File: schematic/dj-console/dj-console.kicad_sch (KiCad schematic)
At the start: 0 parts

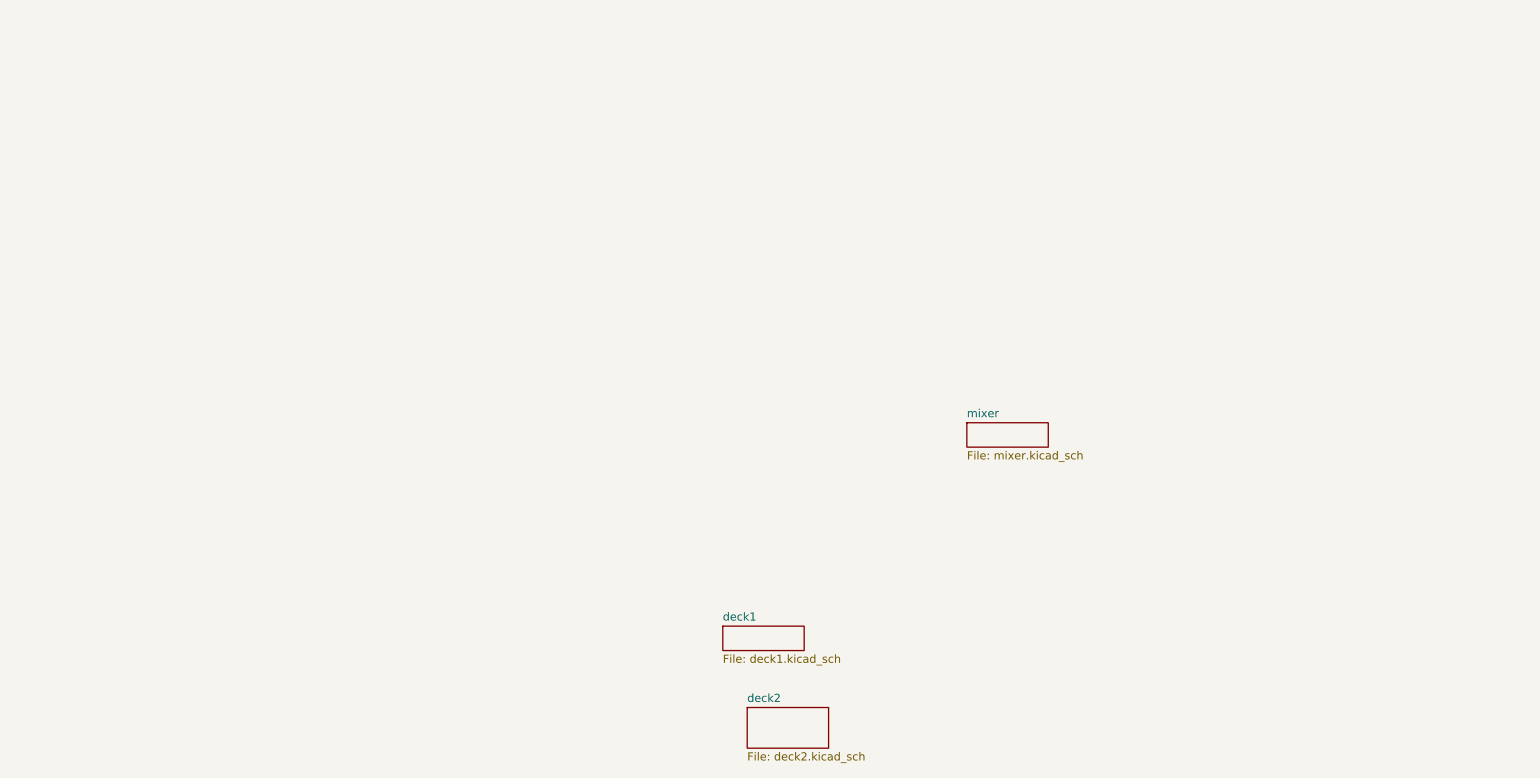
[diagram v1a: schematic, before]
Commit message: Finished DECK circuitry -> to be reviewed; Created hierarchical sheets to avoid redundancy
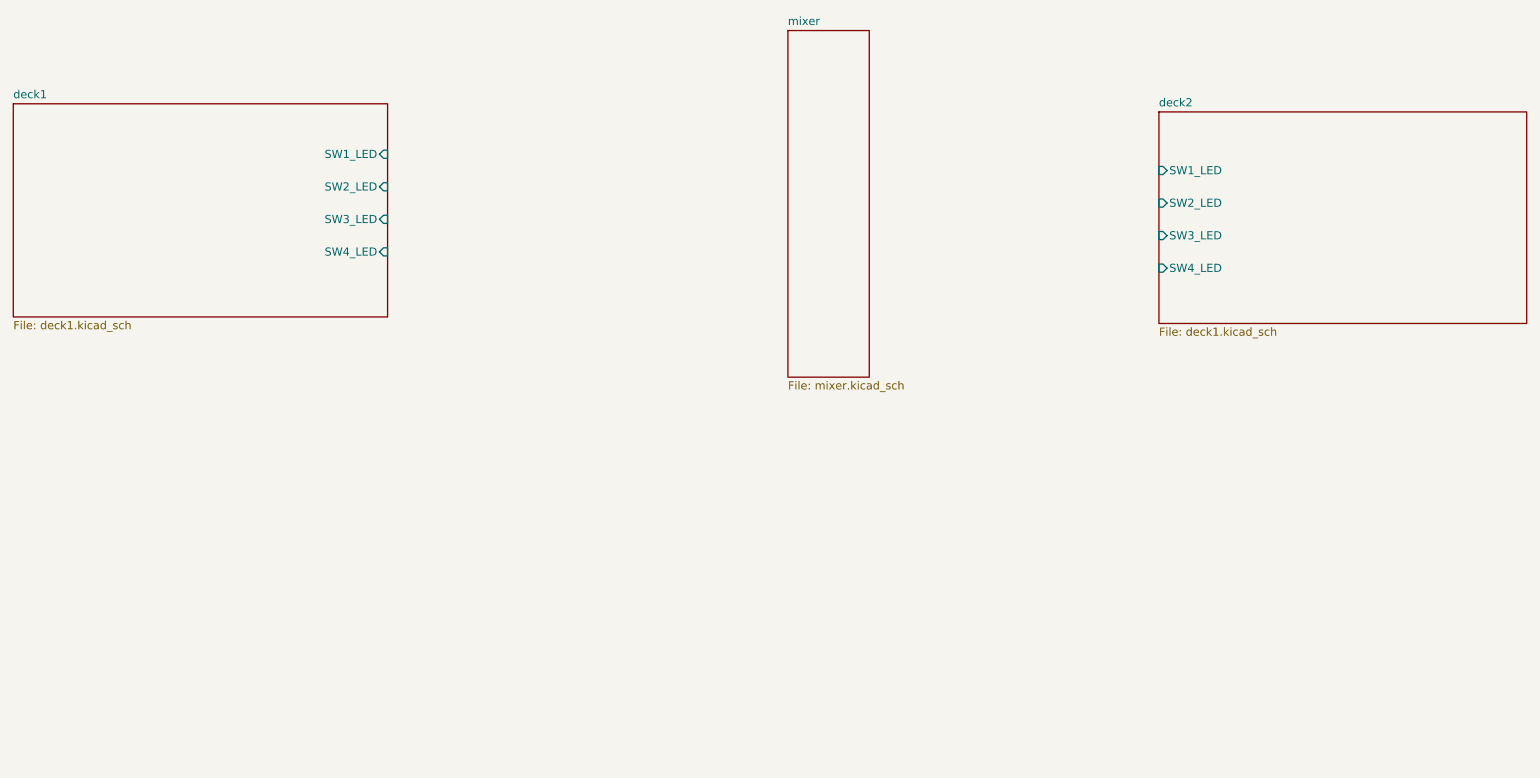
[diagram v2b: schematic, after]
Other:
- sheet deck1 ports: added SW1_LED, SW2_LED, SW3_LED, SW4_LED; removed none
- sheet deck2: file deck2.kicad_sch -> deck1.kicad_sch
- sheet deck2 ports: added SW1_LED, SW2_LED, SW3_LED, SW4_LED; removed none
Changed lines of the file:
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@@
 	)
 	(sheet
-		(at 173.99 135.89)
-		(size 12.7 3.81)
+		(at 203.962 87.376)
+		(size 57.404 33.02)
 		(exclude_from_sim no)
 		(in_bom yes)
@@
 			(color 0 0 0 0)
 		)
-		(property "Sheetname" "mixer"
-			(at 173.99 135.1784 0)
+		(property "Sheetname" "deck2"
+			(at 203.962 86.6644 0)
 			(show_name no)
 			(do_not_autoplace no)
@@
 			)
 		)
-		(property "Sheetfile" "mixer.kicad_sch"
-			(at 173.99 140.2846 0)
+		(property "Sheetfile" "deck1.kicad_sch"
+			(at 203.962 120.9806 0)
 			(show_name no)
 			(do_not_autoplace no)
@@
 				)
 				(justify left top)
+			)
+		)
+		(pin "SW1_LED" input
+			(at 203.962 96.52 180)
+			(effects
+				(font
+					(size 1.27 1.27)
+				)
+				(justify left)
+			)
+		)
+		(pin "SW2_LED" input
+			(at 203.962 101.6 180)
+			(effects
+				(font
+					(size 1.27 1.27)
+				)
+				(justify left)
+			)
+		)
+		(pin "SW3_LED" input
+			(at 203.962 106.68 180)
+			(effects
+				(font
+					(size 1.27 1.27)
+				)
+				(justify left)
+			)
+		)
+		(pin "SW4_LED" input
+			(at 203.962 111.76 180)
+			(effects
+				(font
+					(size 1.27 1.27)
+				)
+				(justify left)
 			)
 		)
@@
 			(project "dj-console"
 				(path "/cbea8acf-e301-41c4-99fc-3eb7e47427af"
-					(page "4")
+					(page "3")
 				)
 			)
@@
 	)
 	(sheet
-		(at 139.7 180.34)
-		(size 12.7 6.35)
+		(at 146.05 74.676)
+		(size 12.7 54.102)
 		(exclude_from_sim no)
 		(in_bom yes)
@@
 			(color 0 0 0 0)
 		)
-		(property "Sheetname" "deck2"
-			(at 139.7 179.6284 0)
+		(property "Sheetname" "mixer"
+			(at 146.05 73.9644 0)
 			(show_name no)
 			(do_not_autoplace no)
@@
 			)
 		)
-		(property "Sheetfile" "deck2.kicad_sch"
-			(at 139.7 187.2746 0)
+		(property "Sheetfile" "mixer.kicad_sch"
+			(at 146.05 129.3626 0)
 			(show_name no)
 			(do_not_autoplace no)
@@
 			(project "dj-console"
 				(path "/cbea8acf-e301-41c4-99fc-3eb7e47427af"
-					(page "3")
+					(page "4")
 				)
 			)
@@
 	)
 	(sheet
-		(at 135.89 167.64)
-		(size 12.7 3.81)
+		(at 25.146 86.106)
+		(size 58.42 33.274)
 		(exclude_from_sim no)
 		(in_bom yes)
@@
 		)
 		(property "Sheetname" "deck1"
-			(at 135.89 166.9284 0)
+			(at 25.146 85.3944 0)
 			(show_name no)
 			(do_not_autoplace no)
@@
 		)
 		(property "Sheetfile" "deck1.kicad_sch"
-			(at 135.89 172.0346 0)
+			(at 25.146 119.9646 0)
 			(show_name no)
 			(do_not_autoplace no)
@@
 			)
 		)
+		(pin "SW1_LED" input
+			(at 83.566 93.98 0)
+			(effects
+				(font
+					(size 1.27 1.27)
+				)
+				(justify right)
+			)
+		)
+		(pin "SW2_LED" input
+			(at 83.566 99.06 0)
+			(effects
+				(font
+					(size 1.27 1.27)
+				)
+				(justify right)
+			)
+		)
+		(pin "SW3_LED" input
+			(at 83.566 104.14 0)
+			(effects
+				(font
+					(size 1.27 1.27)
+				)
+				(justify right)
+			)
+		)
+		(pin "SW4_LED" input
+			(at 83.566 109.22 0)
+			(effects
+				(font
+					(size 1.27 1.27)
+				)
+				(justify right)
+			)
+		)

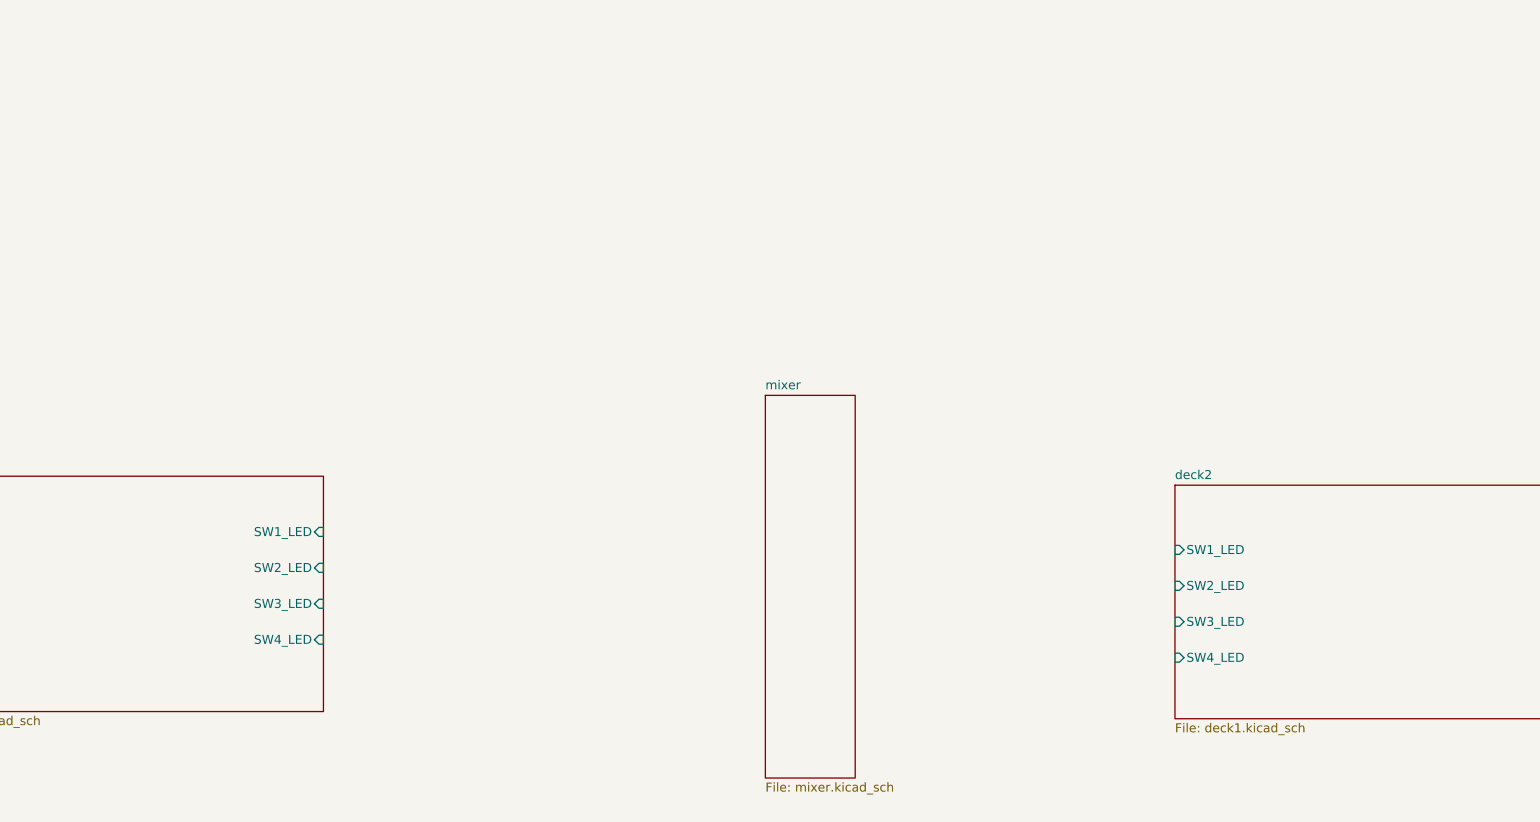
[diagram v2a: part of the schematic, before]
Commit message: Created first version of mixer circuit and added tempo sliders on decks
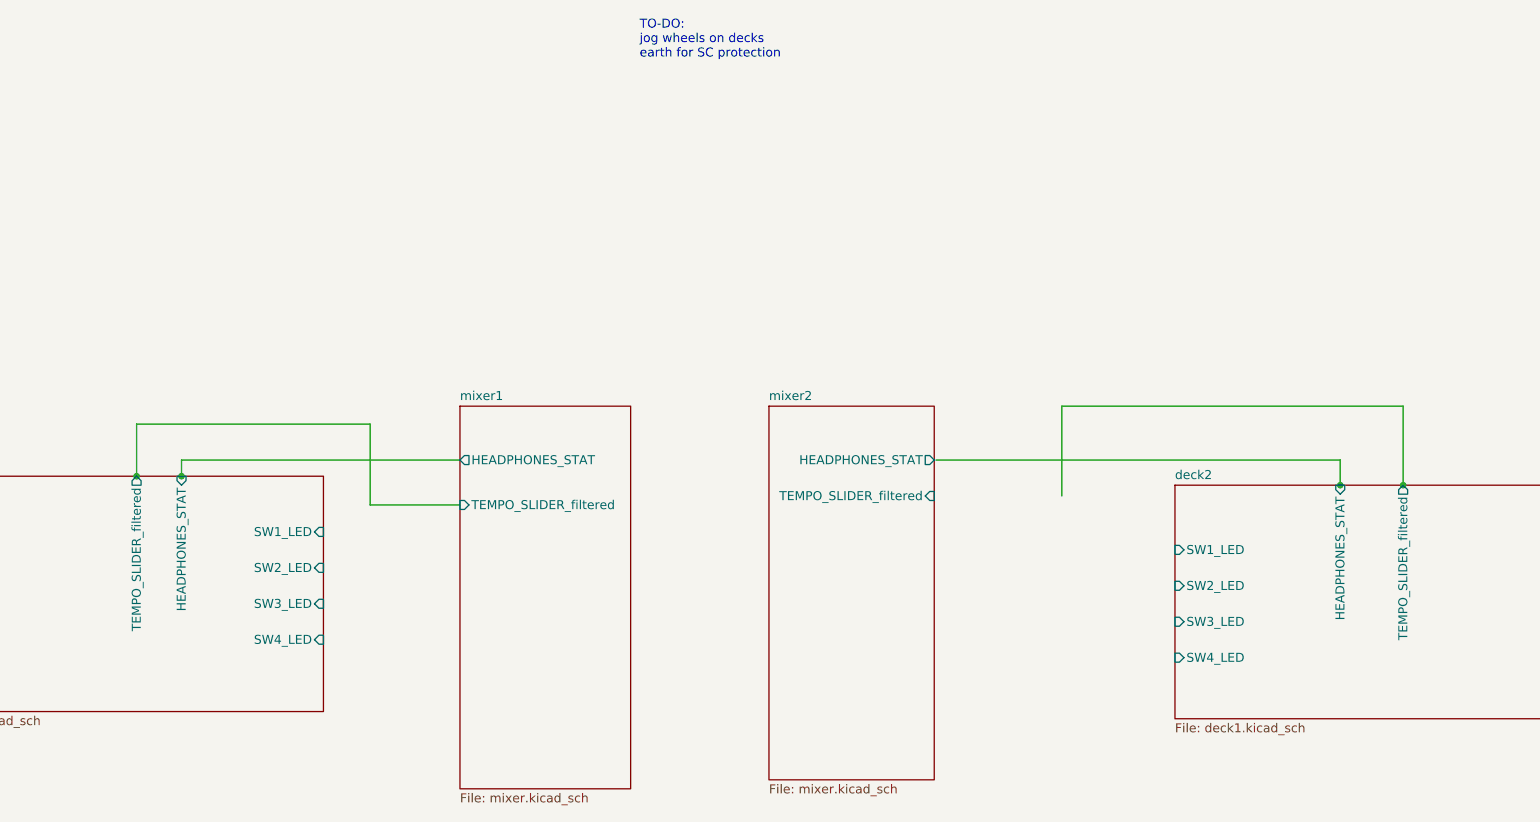
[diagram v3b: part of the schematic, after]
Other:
- sheet mixer renamed mixer1
- added sheet mixer2 (mixer.kicad_sch)
- sheet deck1 ports: added HEADPHONES_STAT, TEMPO_SLIDER_filtered; removed none
- sheet deck2 ports: added HEADPHONES_STAT, TEMPO_SLIDER_filtered; removed none
- sheet mixer1 ports: added HEADPHONES_STAT, TEMPO_SLIDER_filtered; removed none
- note added: "TO-DO: jog wheels on decks earth for SC protection"

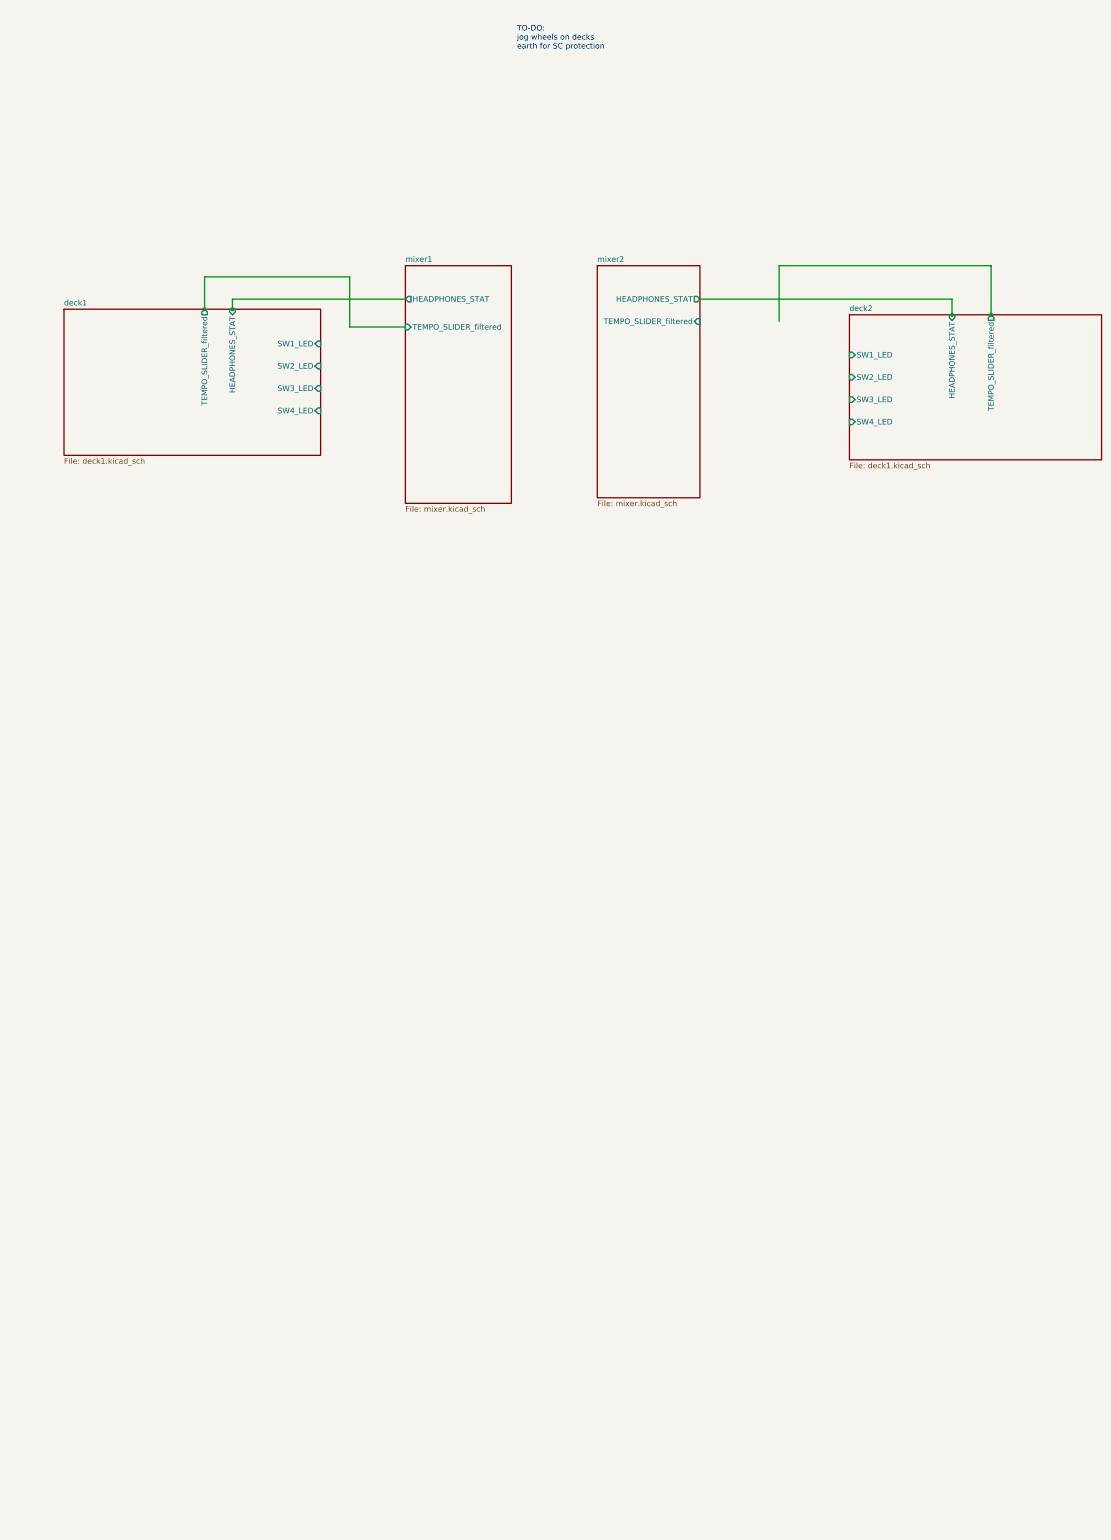
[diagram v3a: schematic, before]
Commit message: Added MASTER and HEADPHONES gain together with crossfader slider
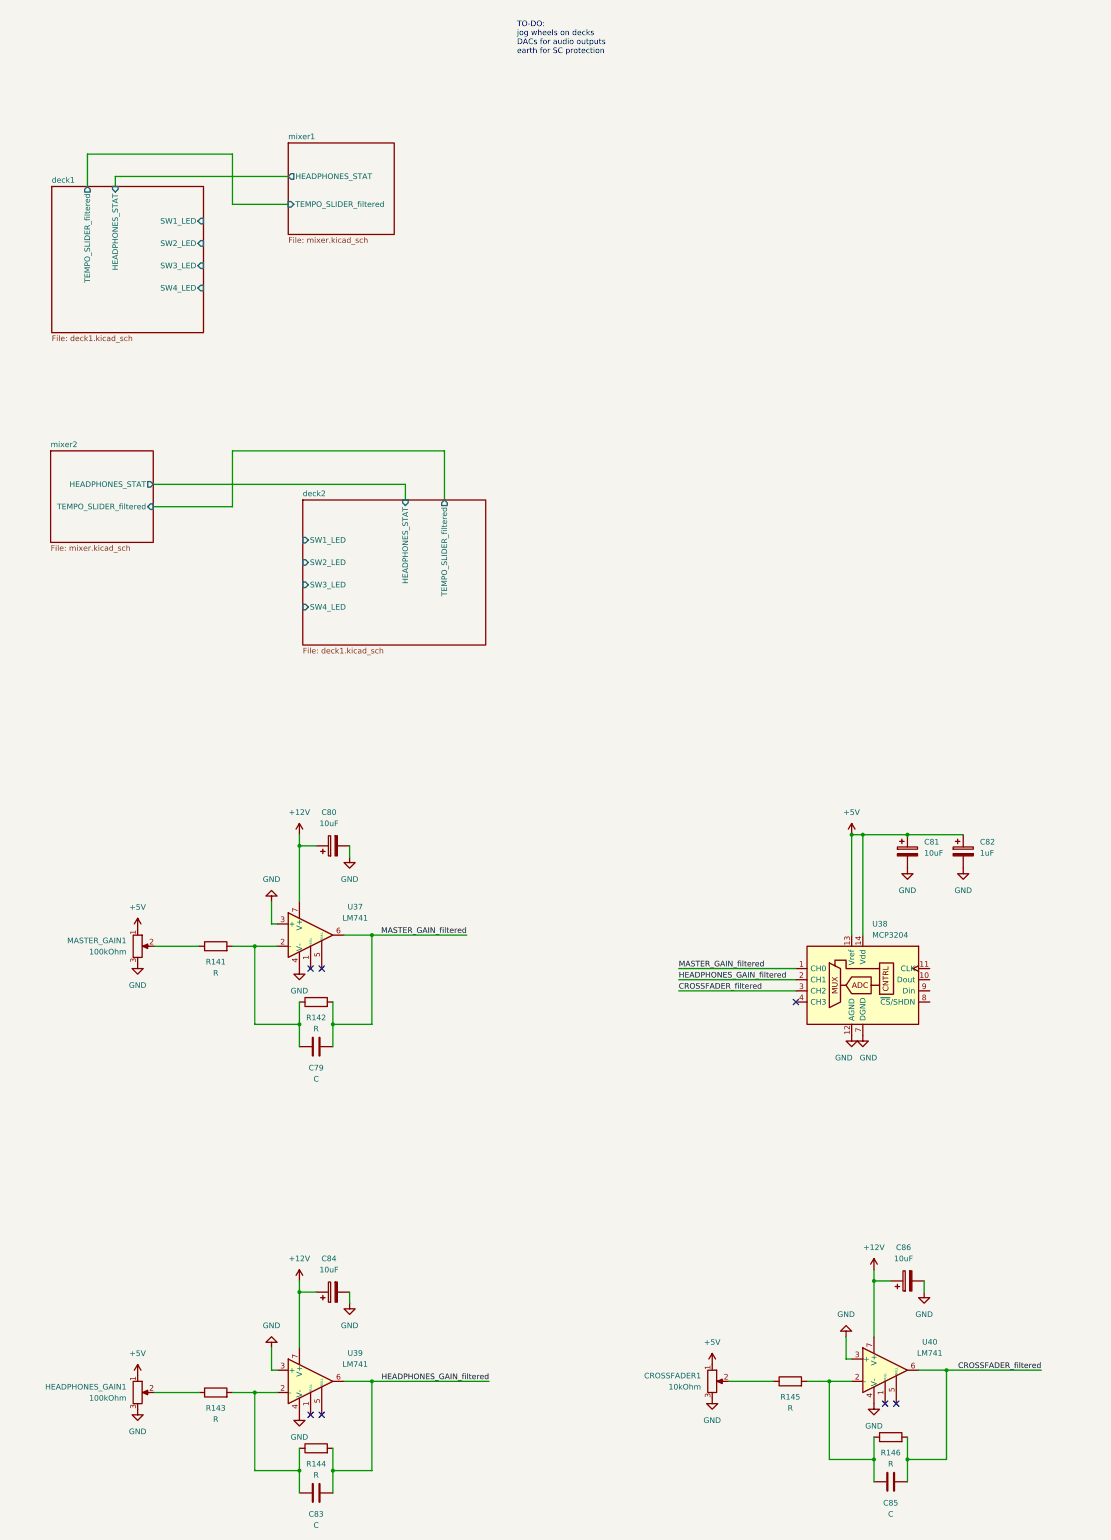
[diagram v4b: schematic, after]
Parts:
- added C79, C83, C85: C, symbol Device:C
- added C80, C81, C84, C86: 10uF, symbol Device:C_Polarized
- added C82: 1uF, symbol Device:C_Polarized
- added CROSSFADER1: 10kOhm, symbol Device:R_Potentiometer
- added HEADPHONES_GAIN1, MASTER_GAIN1: 100kOhm, symbol Device:R_Potentiometer
- added R141, R142, R143, R144, R145, R146: R, symbol Device:R
- added U37, U39, U40: LM741, symbol Amplifier_Operational:LM741
- added U38: MCP3204, symbol Analog_ADC:MCP3204
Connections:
- new net: C85.2, R145.2, R146.1, U40.2 (-)
- new net: HEADPHONES_GAIN1.2, R143.1
- new net: C83.2, R143.2, R144.1, U39.2 (-)
- new net: CROSSFADER1.2, R145.1
- new net: C79.2, R141.2, R142.1, U37.2 (-)
- new net: MASTER_GAIN1.2, R141.1
- new net +12V: C80.1, C84.1, C86.1, U37.7 (V+), U39.7 (V+), U40.7 (V+)
- new net +5V: C81.1, C82.1, CROSSFADER1.1, HEADPHONES_GAIN1.1, MASTER_GAIN1.1, U38.13 (Vref), U38.14 (Vdd)
- new net CROSSFADER_filtered: C85.1, R146.2, U38.3 (CH2), U40.6
- new net GND: C80.2, C81.2, C82.2, C84.2, C86.2, CROSSFADER1.3, HEADPHONES_GAIN1.3, MASTER_GAIN1.3, U37.3 (+), U37.4 (V-), U38.12 (AGND), U38.7 (DGND), U39.3 (+), U39.4 (V-), U40.3 (+), U40.4 (V-)
- new net HEADPHONES_GAIN_filtered: C83.1, R144.2, U38.2 (CH1), U39.6
- new net MASTER_GAIN_filtered: C79.1, R142.2, U37.6, U38.1 (CH0)
- no-connect marks 0 -> 7
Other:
- note added: "TO-DO: jog wheels on decks DACs for audio outputs earth for SC protection"
- note removed: "TO-DO: jog wheels on decks earth for SC protection"
